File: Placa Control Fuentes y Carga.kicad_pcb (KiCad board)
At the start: 2 copper layers, 160 x 95 mm, 139 parts, among them J1 TBP01R1-508-02BE, J10 TBP01R1-508-03BE, J2 TBP01R1-508-02BE, J3 TBP01R1-508-02BE, J4 TBP01R1-508-02BE, J5 TBP01R1-508-02BE, J6 TBP01R1-508-02BE, J7 TBP01R1-508-02BE, J8 TBP01R1-508-02BE, J9 TBP01R1-508-02BE, Q1 IRF9540N, Q2 2N3904, Q3 BC558, Q4 BC558, Q5 IRF5305, Q6 BC337, Q7 BC327, U1 ACS724LLCTR-05AB-T, U2 Relay_Module_WB-083, U3 4N35, U4 LM2596S_Modulo_Regulable, U5 Arduino_Nano_ATmega328P, U6 ACS724LLCTR-05AB-T, U7 MAX485E, U8 MAX22445FAWE+, U9 RI3-0505S

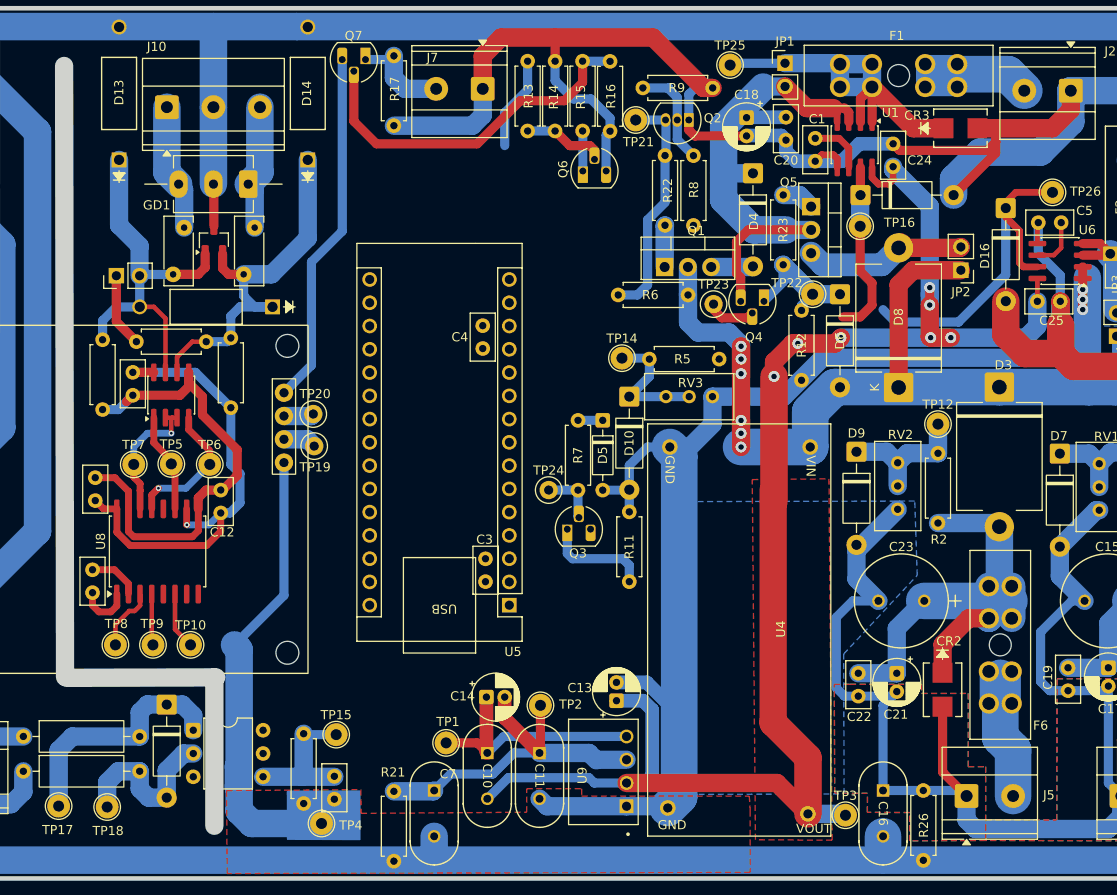
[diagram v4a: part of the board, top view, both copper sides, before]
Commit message: wip(pcb): ruteo 58/76 (falta ADC0); GND_B sin plano; barrera 220VCA e IPC pendientes.
feat(pcb): ruteo casi cerrado (solo falta ADC0) + refuerzo de vias

== Avances mas notables ==
- Ruteo: 858 segmentos (340 F.Cu / 518 B.Cu) + 33 vias (+14 vs commit previo)
- 58/76 nets ruteadas; PWM ya ruteado -> unica senal real pendiente: ADC0
- GND densificado (182 seg); +5V (87 seg) completado
- Dominio aislado RS-485 cableado: GND_B (45 seg) y +5V_B (29 seg)
- Earth de proteccion ancho (3-5 mm, 22 seg)
- Planos rellenados (locked): GND x4 (masa1-4, F.Cu+B.Cu), +5V (F.Cu), +12V (B.Cu)
- 9 keepouts de aislamiento en F.Cu

== Pendiente para finalizar ==
- Rutear ADC0; dejar ratsnest en cero
- GND_B/+5V_B siguen solo como pistas: definir isla/retorno vertido de
  GND_B (hoy NO existe zona de cobre para el retorno aislado)
- Verificar separacion GND vs GND_B (sin cruces ni acoplamiento)
- Seguir reforzando via stitching en planos GND (33 vias)
- Barrera 220 VCA: confirmar ranura de fresado bajo U3 (4N35) y fijar
  creepage/clearance (faltan: clase de aislamiento, recubrimiento, polucion)
- Validar anchos vs IPC-2152 con corrientes reales
- Confirmar stackup/peso de cobre (1 oz?), DRC limpio y serigrafia.
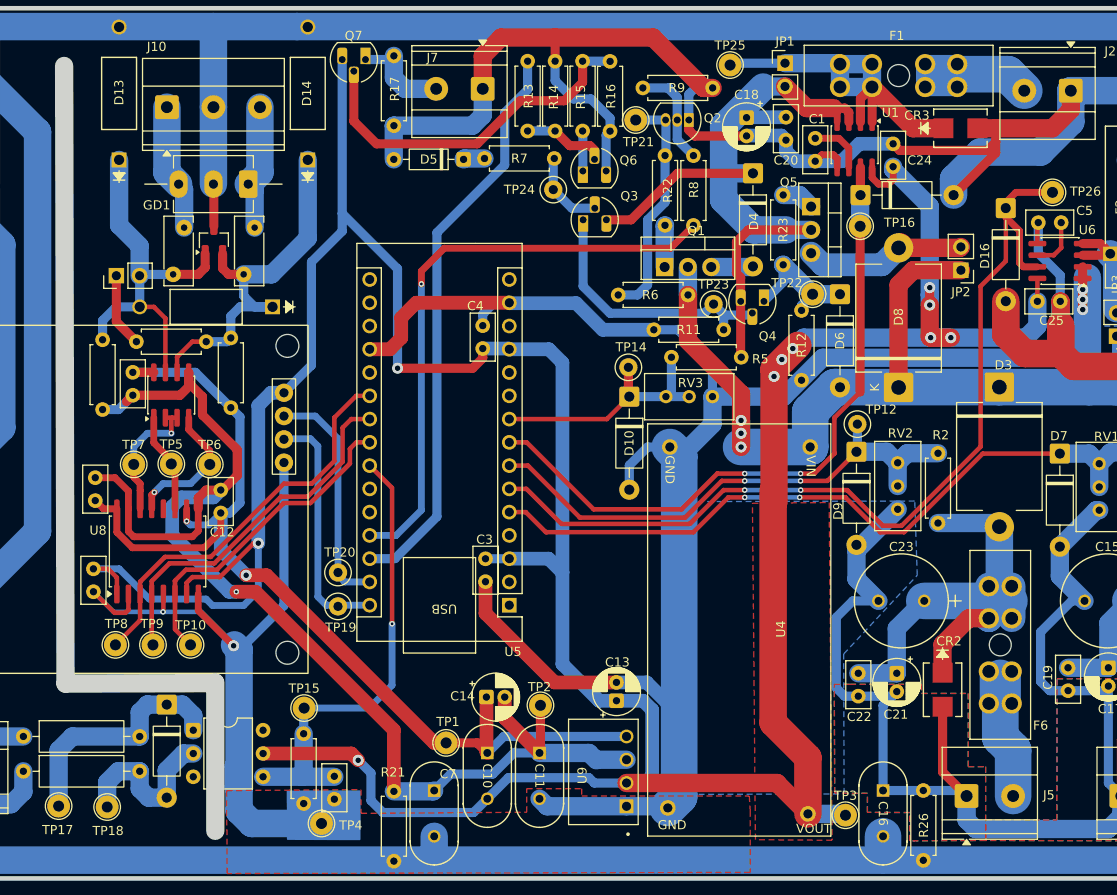
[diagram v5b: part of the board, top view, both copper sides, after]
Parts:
- moved R7 36.3 mm to (141.6, 71.4), turned to 180 degrees
- moved Q3 33.8 mm to (144.8, 78.1)
- moved TP24 32.8 mm to (141.5, 74.8)
- moved D5 32.3 mm to (131.7, 71.5), turned to 180 degrees
- moved R11 29.4 mm to (160.1, 90.1), turned to 180 degrees
- moved TP19 17.7 mm to (118.0, 120.3)
- moved TP20 17.5 mm to (118.0, 116.6)
- moved TP12 8.80 mm to (174.7, 100.4)
- moved TP15 4.55 mm to (114.3, 131.4)
- moved C8 2.60 mm to (91.3, 116.2), turned to -90 degrees
- moved R5 2.42 mm to (162.0, 93.1)
- moved TP14 1.22 mm to (149.7, 94.2)
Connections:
- D10 pad 1: ADC3 -> ADC5
- D16 pad 1: ADC5 -> ADC2
- D9 pad 1: ADC2 -> ADC3
- R2 pad 2: ADC2 -> ADC3
- R5 pad 2: ADC3 -> ADC5
- RV2 pad 1: ADC2 -> ADC3
- RV2 pad 2: ADC2 -> ADC3
- RV3 pad 2: ADC3 -> ADC5
- RV3 pad 3: ADC3 -> ADC5
- TP12 pad 1: ADC2 -> ADC3
- TP14 pad 1: ADC3 -> ADC5
- TP26 pad 1: ADC5 -> ADC2
- U5 pad 20: DE/RE -> unconnected-(U5-D2-Pad20)
- U5 pad 21: unconnected-(U5-D3-Pad21) -> DE/RE
- U6 pad 7: ADC5 -> ADC2
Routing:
- net +5V: track 218.7 -> 395.0 mm, vias 7 -> 10
- net GND: track 584.9 -> 684.6 mm, vias 0 -> 2
- net ADC2: track 15.5 -> 102.0 mm, vias 0 -> 2
- net ADC1: track 15.2 -> 82.9 mm, vias 0 -> 2
- net PWM: track 0.00 -> 64.6 mm, vias 0 -> 1
- net ADC4: track 19.3 -> 73.5 mm, vias 0 -> 2
- net F220_OUT: track 10.3 -> 63.1 mm
- net GND_B: track 92.4 -> 141.2 mm, vias 0 -> 1
- net ADC3: track 14.6 -> 58.5 mm, vias 0 -> 2
- net +5V_B: track 80.9 -> 118.2 mm, vias 1 -> 2
- net DE/RE: track 7.02 -> 44.3 mm
- net F220_IN: track 16.2 -> 51.1 mm, vias 0 -> 1
- net DI: track 5.61 -> 40.3 mm
- net RO: track 6.25 -> 36.2 mm
- net Net-(D4-K): track 62.1 -> 86.3 mm
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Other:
- outline, holes or cut-outs redrawn
